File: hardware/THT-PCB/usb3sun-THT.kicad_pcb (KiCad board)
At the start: 2 copper layers, 83.9 x 40.6 mm, 46 parts, among them J2 8918-P8B, J3 USB-U267-BWS, Q1 2N7000, Q2 2N7000, Q3 2N7000, Q4 2N7000, Q5 2N7000, Q6 2N7000, SW1 TS665CJ, U1 Pico, U2 SRV05-4, U4 MAX40200AUK, U5 MAX40200AUK

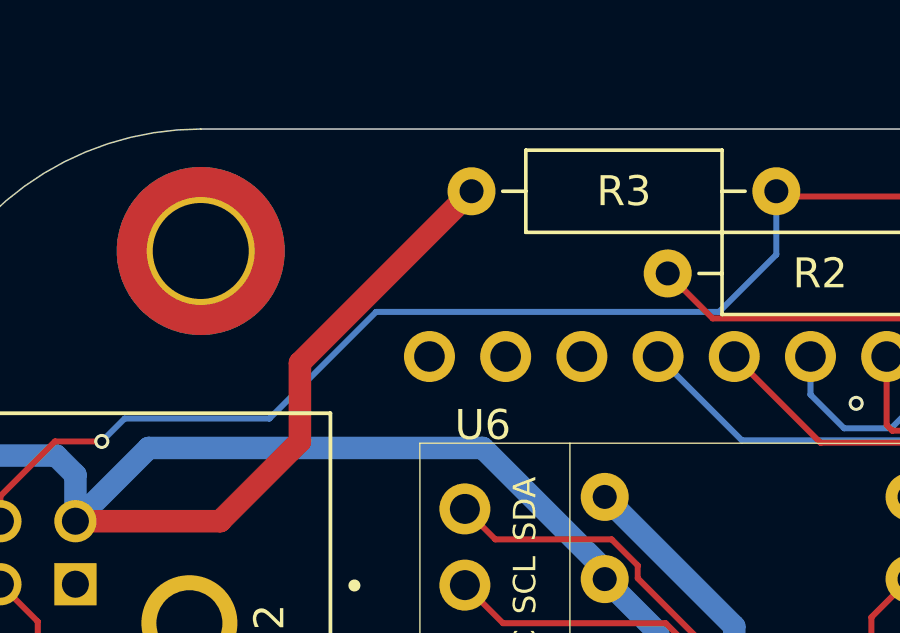
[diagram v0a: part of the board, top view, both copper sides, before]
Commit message: Add UART Header
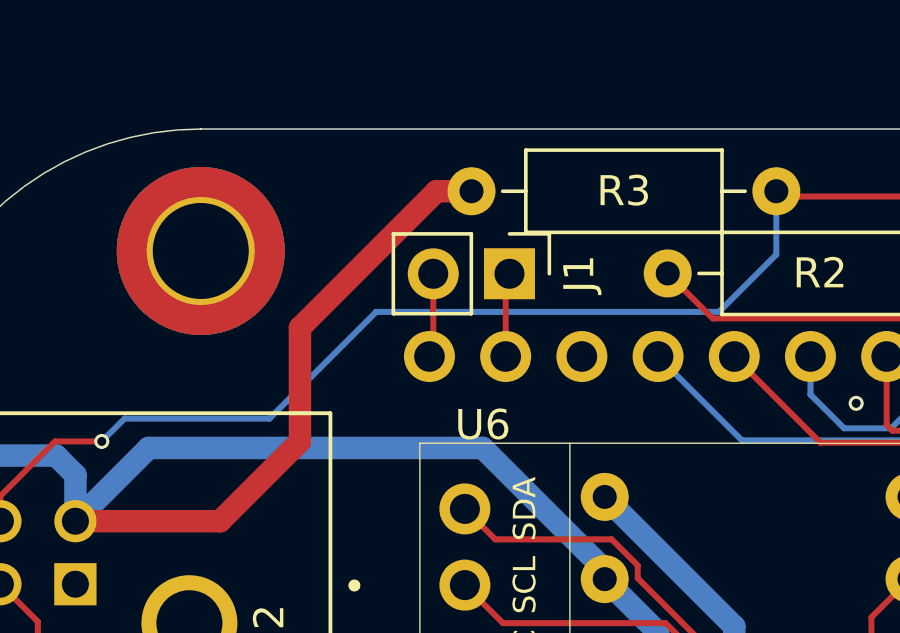
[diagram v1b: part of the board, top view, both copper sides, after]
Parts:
- added J1: Conn_01x02, Connector_PinHeader_2.54mm:PinHeader_1x02_P2.54mm_Vertical, F.Cu at (81.9, 48.3)
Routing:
- net /UART_RX: track 0.00 -> 2.81 mm
- net /UART_TX: track 0.00 -> 2.81 mm
- net VSUN: track 122.0 -> 122.7 mm

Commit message: PCB work
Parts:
- added REF**: OSHW-Symbol_6.7x6mm_SilkScreen, Symbol:OSHW-Symbol_6.7x6mm_SilkScreen, F.Cu at (82.8, 73.7)
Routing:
- net /BUZZER: track 20.8 -> 21.8 mm
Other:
- board text added: "5v"
- board text added: "GND"
- board text added: "Power"
- board text added: "RX"
- board text added: "TX"

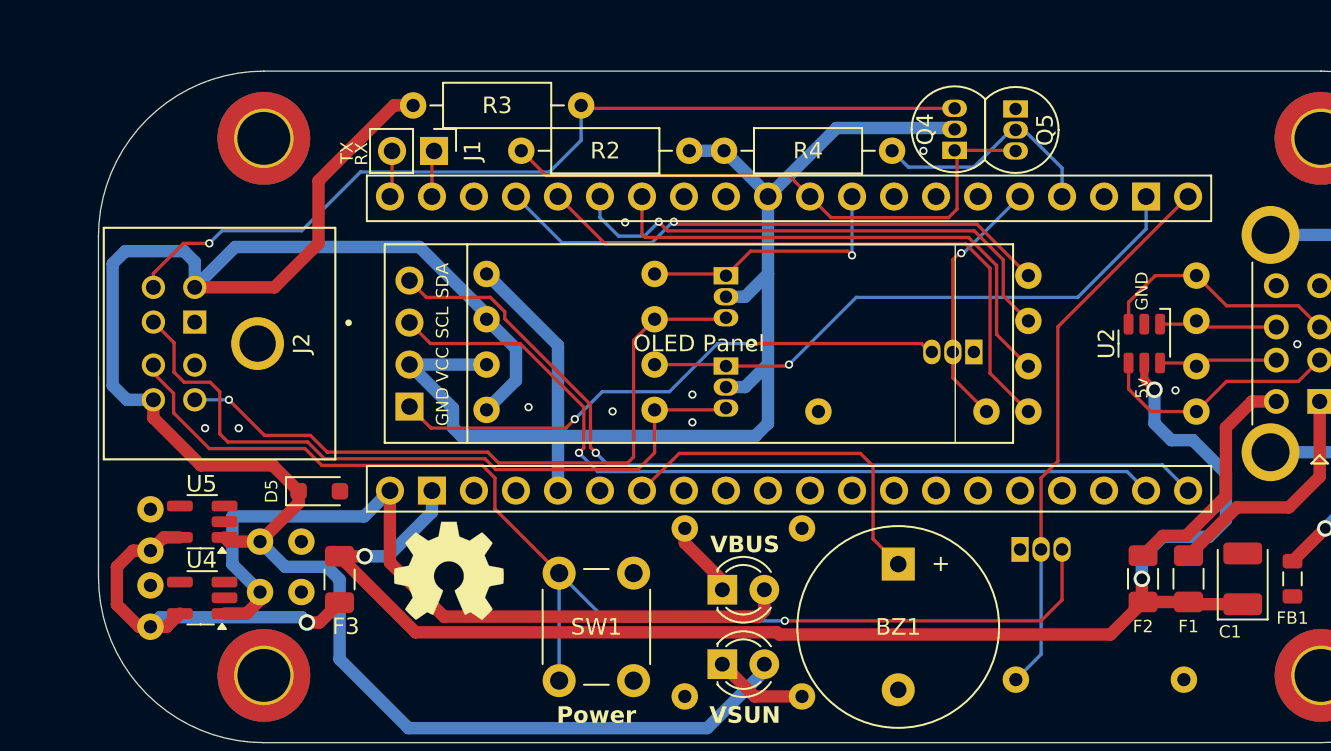
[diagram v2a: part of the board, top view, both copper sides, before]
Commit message: Fix Sun connector, add connector config jumpers
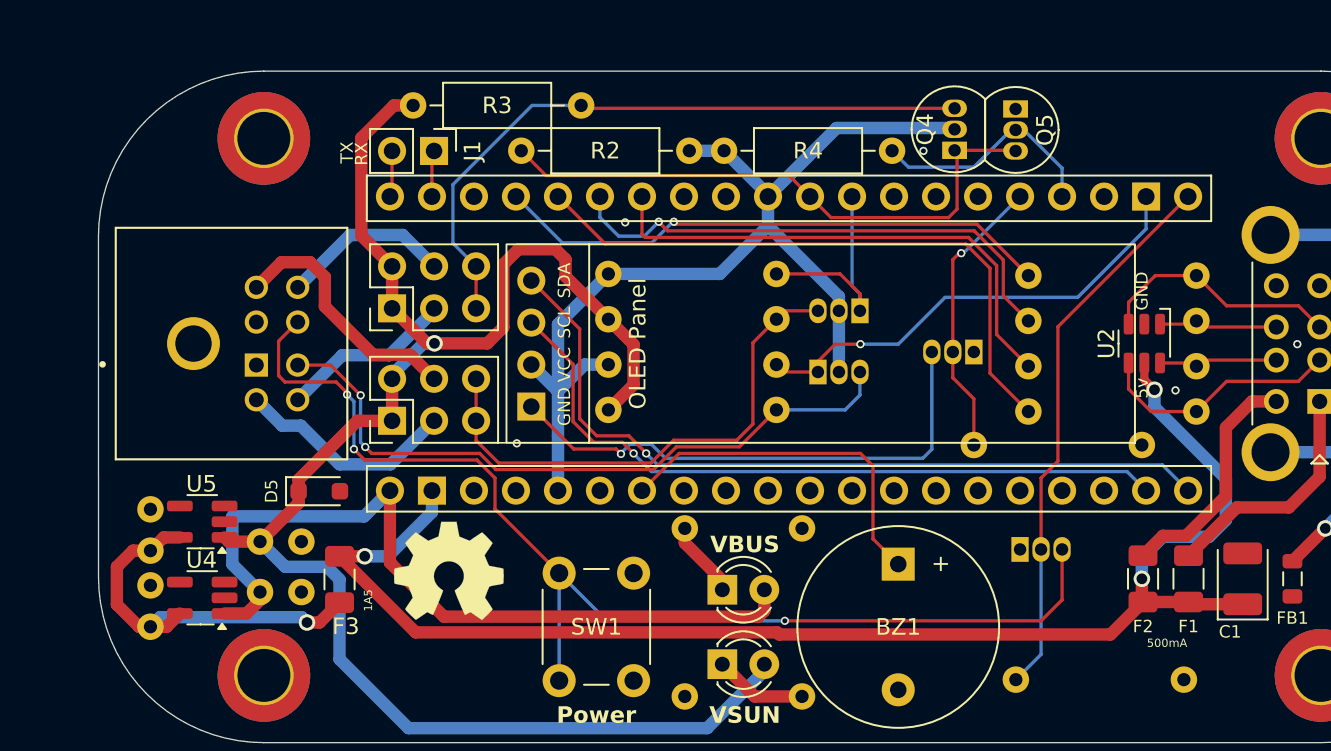
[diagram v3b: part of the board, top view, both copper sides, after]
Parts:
- added J4: Conn_02x03_Odd_Even, Connector_PinHeader_2.54mm:PinHeader_2x03_P2.54mm_Vertical, F.Cu at (79.4, 64.6)
- added J5: Conn_02x03_Odd_Even, Connector_PinHeader_2.54mm:PinHeader_2x03_P2.54mm_Vertical, F.Cu at (79.4, 57.8)
- moved J2 13.3 mm to (62.7, 59.9), turned to -90 degrees
- moved Q2 8.37 mm to (107.7, 57.9), turned to 180 degrees
- moved R5 7.37 mm to (92.5, 55.7)
- moved R6 7.37 mm to (92.5, 61.2)
- moved R8 7.37 mm to (92.5, 63.9)
- moved R9 7.37 mm to (92.5, 58.4)
- moved U6 7.37 mm to (124.3, 65.9)
- moved Q3 5.57 mm to (105.1, 61.6), turned to 0 degrees
- moved R1 2.16 mm to (114.6, 66.0), turned to 0 degrees
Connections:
- J2 pad 3: VSUN -> /PIN3
- J2 pad 5: /KRX -> /PIN5
- J2 pad 6: /KTX -> /PIN6
- J2 pad 8: VSUN -> /PIN8
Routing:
- net +3V3: track 88.8 -> 62.6 mm
- net VSUN: track 122.7 -> 102.9 mm, vias 0 -> 1
- net /PIN5: track 0.00 -> 15.3 mm
- net /KTX: track 54.8 -> 40.5 mm, vias 1 -> 0
- net /PIN3: track 0.00 -> 13.5 mm
- net /PIN6: track 0.00 -> 10.6 mm
- net /PIN8: track 0.00 -> 10.3 mm
- net /KRX: track 41.5 -> 31.6 mm, vias 1 -> 0
- net /DISPLAY_SCL: track 50.8 -> 43.4 mm
- net /INT_MTX: track 35.1 -> 28.5 mm
- net /DISPLAY_SDA: track 54.1 -> 48.2 mm
- net /SPOWER: track 73.5 -> 70.2 mm, vias 1 -> 3
- net /INT_KRX: track 16.4 -> 13.7 mm, vias 1 -> 0
- net /MTX: track 43.9 -> 41.5 mm, vias 0 -> 2
- net /DISPLAY_GND: track 34.5 -> 32.1 mm, vias 2 -> 1
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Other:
- board text added: "1A5"
- board text added: "500mA"
